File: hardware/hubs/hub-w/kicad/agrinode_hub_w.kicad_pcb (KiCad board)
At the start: 2 copper layers, 114 x 96 mm, 101 parts, among them J1 DC 12V 5.5/2.1, J2 DC IN 7-24V, J3 SOLAR 6-24V, J4 USB 5V / PROG, J5 BAT NTC 10k, J6 PROG, J7 I2C, J8 LED STRIP WS2813, J9 RS-485, Q1 AO3401A, Q2 AO3401A, Q3 MMBT3904, Q4 MMBT3904, Q5 BSS138, Q6 MMBT3904, SW1 RESET, SW2 BOOT / PAIR, U1 LM2596S-5.0, U2 TP4056, U3 MIC29302WU, U4 ESP32-WROOM-32E-N8, U5 CH340C, U6 DS3231MZ, U7 MAX3485ESA

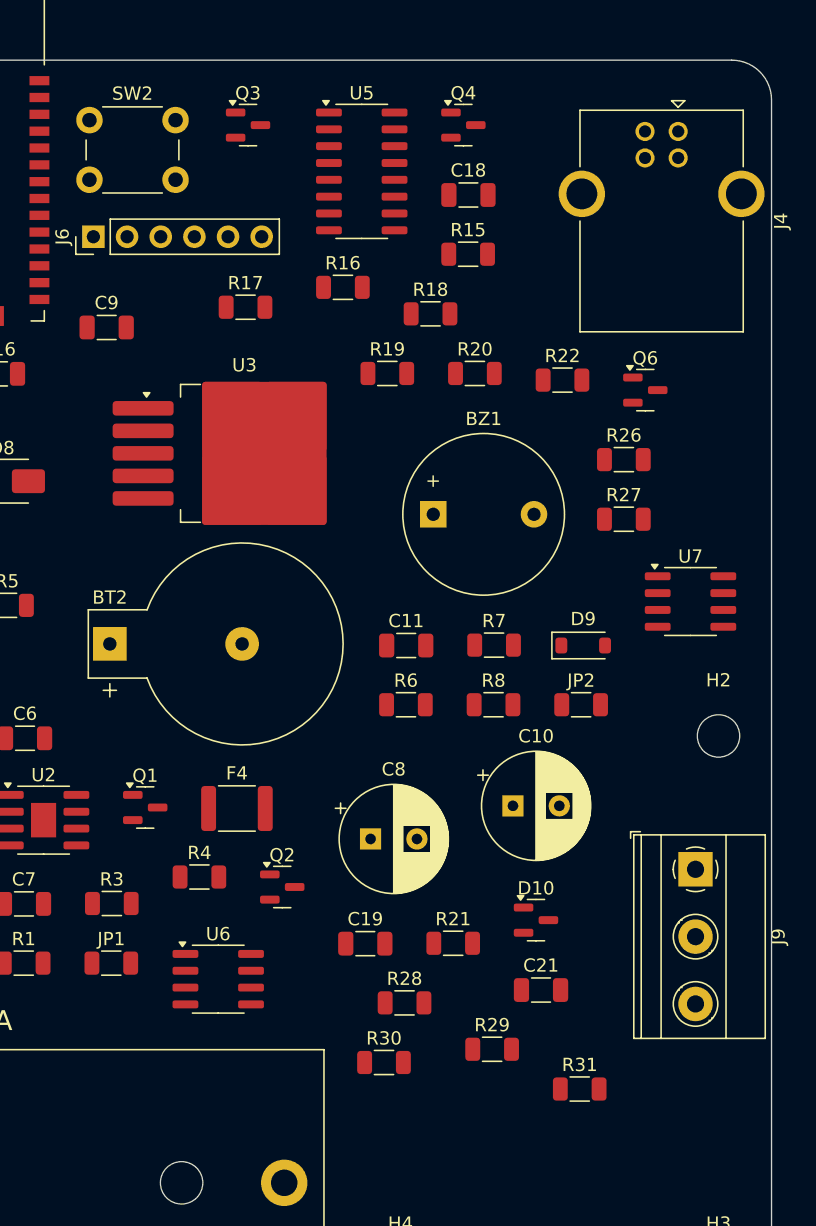
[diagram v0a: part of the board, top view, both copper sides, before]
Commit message: hubs: CH340C rotated so USB D+/D- face the USB-B jack; reroute in progress
Co-Authored-By: Claude Opus 5.5 <noreply@anthropic.com>
Claude-Session: https://claude.ai/code/session_014J7amXZ5Y6AZWEh5CjDNja
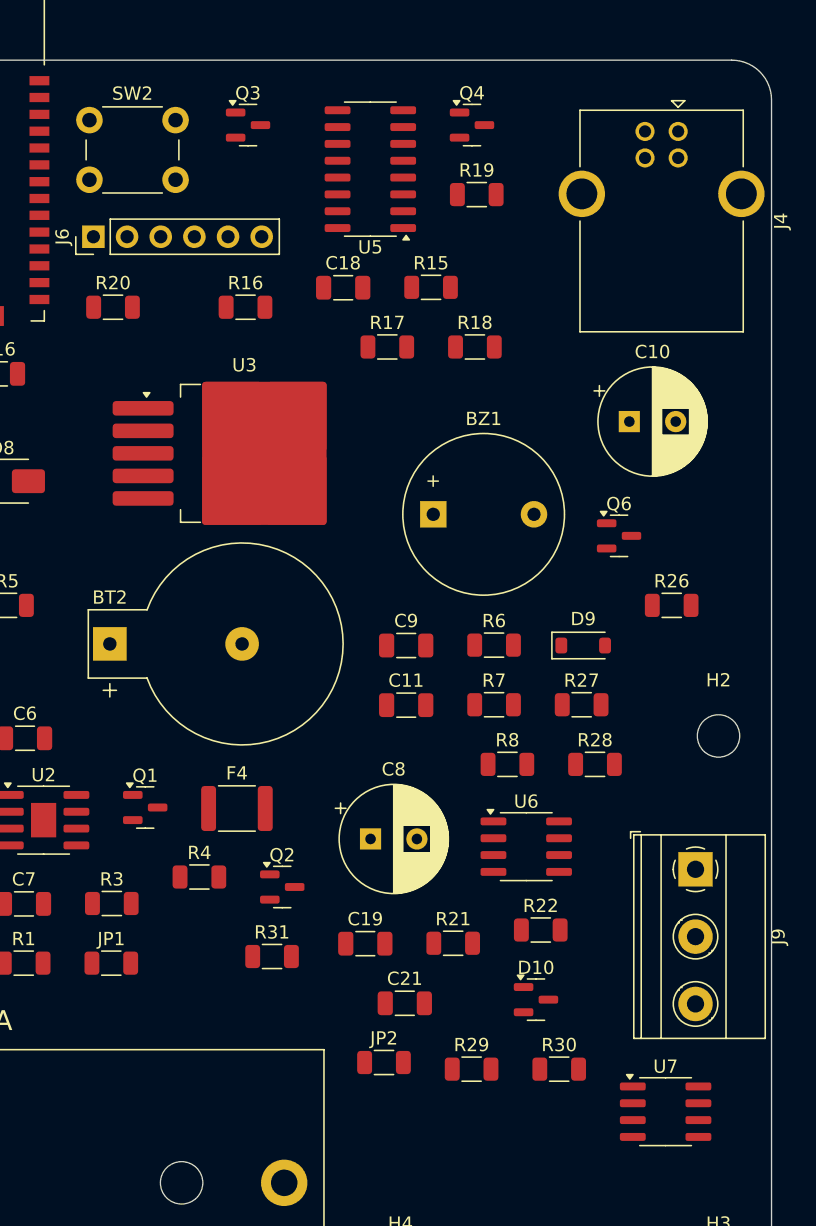
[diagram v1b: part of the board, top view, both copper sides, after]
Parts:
- moved R22 41.5 mm to (146.6, 115.6)
- moved U7 38.5 mm to (156.0, 129.4)
- moved C9 33.0 mm to (136.4, 94.2)
- moved JP2 30.8 mm to (134.8, 125.6)
- moved C10 30.3 mm to (153.3, 77.3)
- moved R20 27.8 mm to (114.3, 68.6)
- moved U6 25.3 mm to (145.5, 109.4)
- moved R31 25.3 mm to (126.3, 117.6)
- moved R28 23.0 mm to (150.7, 103.1)
- moved R19 15.1 mm to (141.8, 60.1)
- moved R27 14.4 mm to (149.7, 98.6)
- moved R30 13.2 mm to (148.0, 126.1)
- moved C18 11.8 mm to (131.7, 67.2)
- moved R26 11.6 mm to (156.5, 91.1)
- moved Q6 11.2 mm to (152.5, 85.9)
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
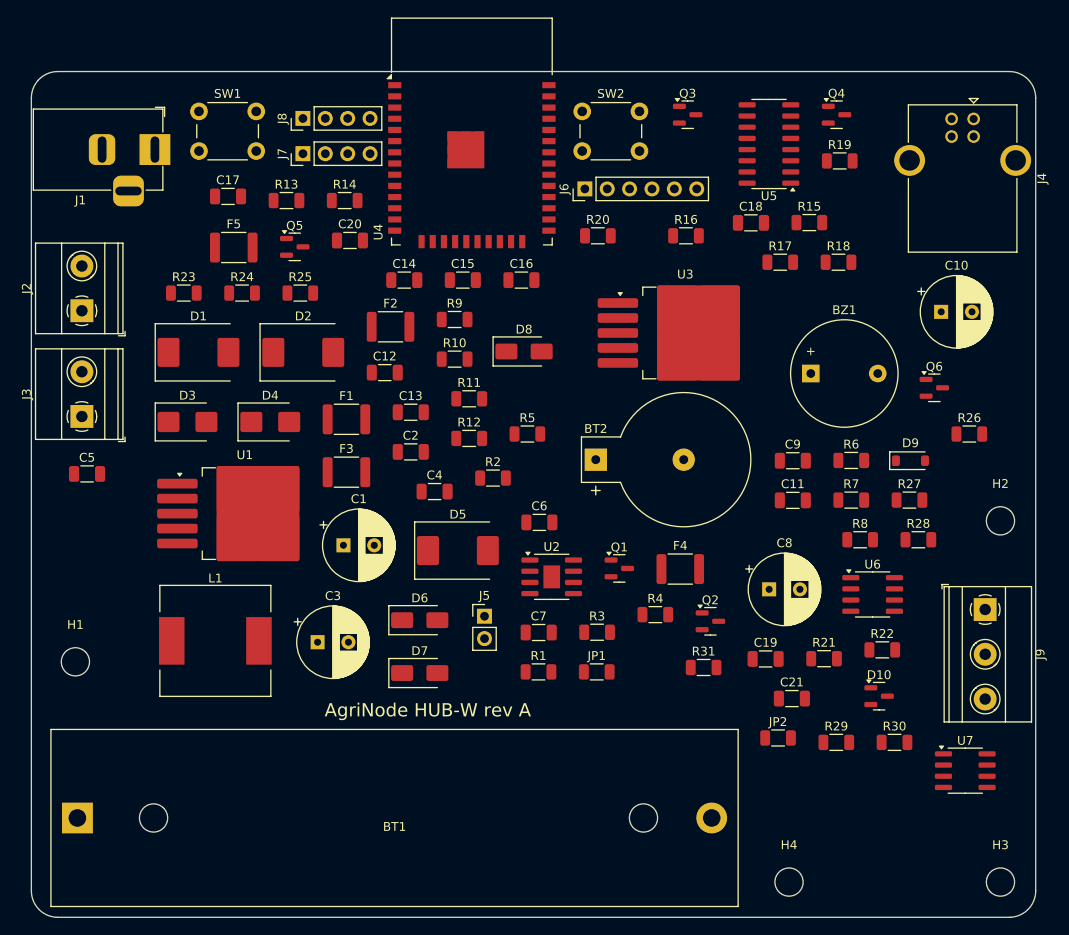
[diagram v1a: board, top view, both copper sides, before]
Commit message: hubs: routing progress snapshot (HUB-W 2 open, HUB-L 3 open)
Co-Authored-By: Claude Opus 5.5 <noreply@anthropic.com>
Claude-Session: https://claude.ai/code/session_014J7amXZ5Y6AZWEh5CjDNja
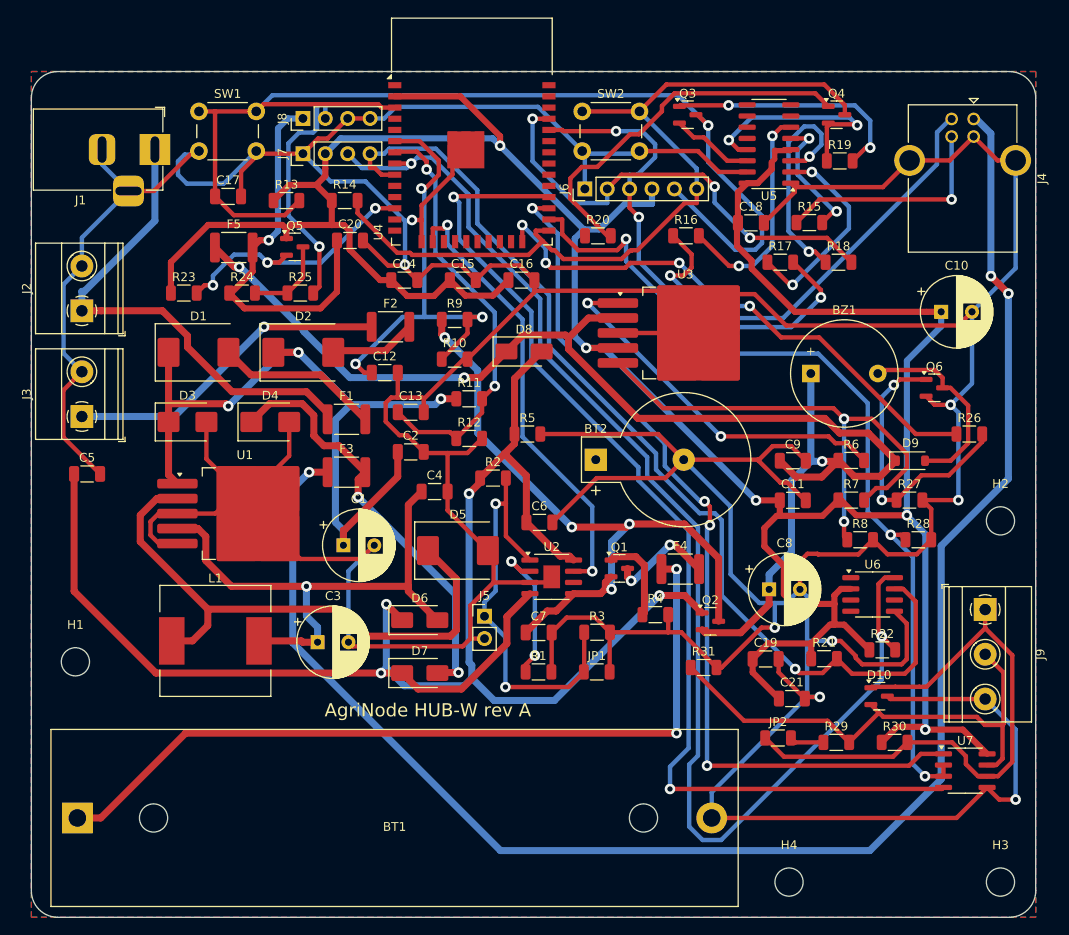
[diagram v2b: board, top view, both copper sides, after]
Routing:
- net GND: track 0.00 -> 802.5 mm, vias 0 -> 8
- net +3V3: track 0.00 -> 343.1 mm, vias 0 -> 5
- net /Power - 12V, solar and USB inputs, 18650 charger, rails/VUSB_RAW: track 0.00 -> 188.9 mm, vias 0 -> 3
- net /Power - 12V, solar and USB inputs, 18650 charger, rails/V5: track 0.00 -> 187.0 mm, vias 0 -> 4
- net VSYS: track 0.00 -> 155.3 mm, vias 0 -> 3
- net /ESP32, programming, buttons, RTC, LED strip, buzzer/I2C_SCL: track 0.00 -> 146.8 mm, vias 0 -> 2
- net /ESP32, programming, buttons, RTC, LED strip, buzzer/ESP_EN: track 0.00 -> 127.9 mm, vias 0 -> 1
- net RS485_TX: track 0.00 -> 121.1 mm, vias 0 -> 2
- net /ESP32, programming, buttons, RTC, LED strip, buzzer/I2C_SDA: track 0.00 -> 115.1 mm, vias 0 -> 1
- net RS485_RX: track 0.00 -> 101.3 mm, vias 0 -> 4
- net RS485_DE: track 0.00 -> 98.8 mm, vias 0 -> 3
- net /ESP32, programming, buttons, RTC, LED strip, buzzer/BOOT_BTN: track 0.00 -> 95.3 mm
- net /Power - 12V, solar and USB inputs, 18650 charger, rails/BATT_CELL: track 0.00 -> 92.3 mm, vias 0 -> 2
- net /Power - 12V, solar and USB inputs, 18650 charger, rails/VIN_BUCK: track 0.00 -> 86.5 mm, vias 0 -> 3
- net /Power - 12V, solar and USB inputs, 18650 charger, rails/VBAT: track 0.00 -> 77.0 mm, vias 0 -> 4
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- added copper zone on B.Cu, net GND
- added copper zone on F.Cu, net GND

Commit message: hubs: place DS3231 beside the CR2032 holder
Co-Authored-By: Claude Opus 5.5 <noreply@anthropic.com>
Claude-Session: https://claude.ai/code/session_014J7amXZ5Y6AZWEh5CjDNja
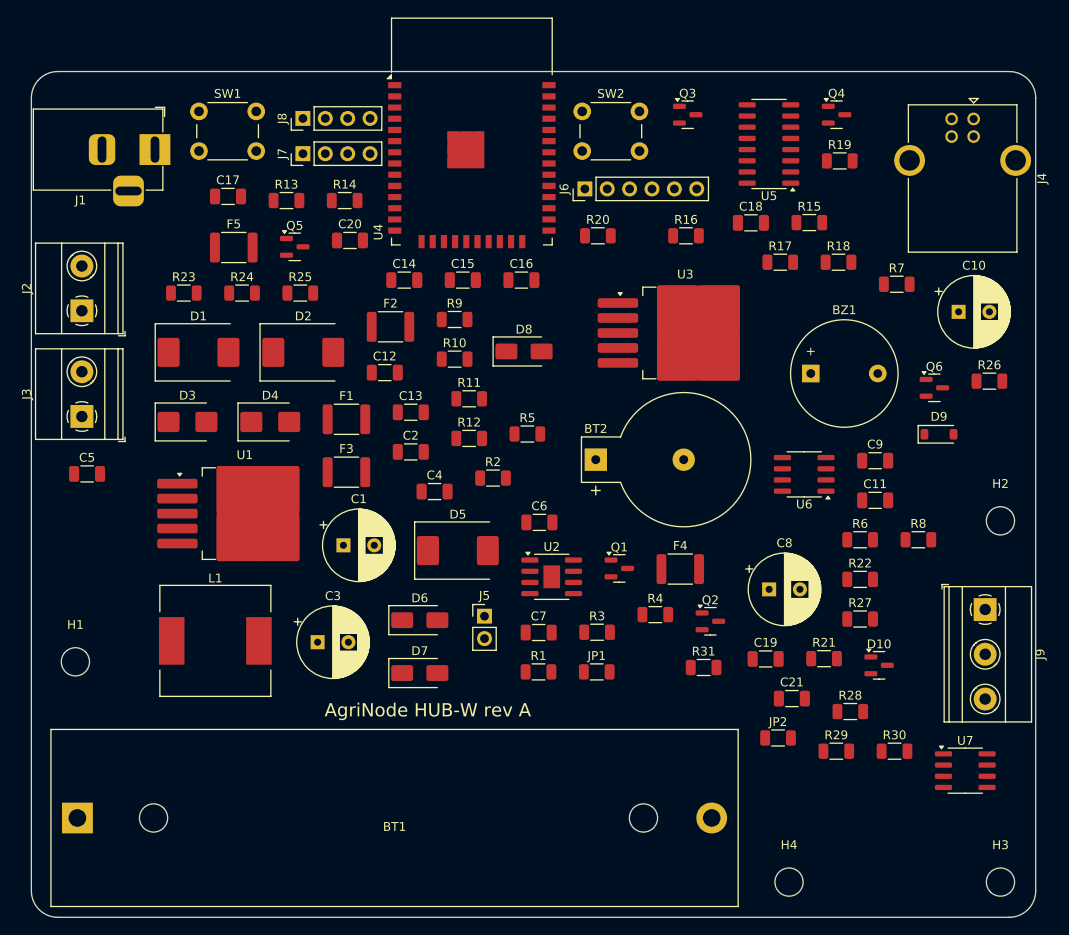
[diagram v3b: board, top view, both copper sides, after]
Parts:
- moved R7 25.0 mm to (148.2, 74.1)
- moved R28 21.0 mm to (143.0, 122.6)
- moved U6 15.7 mm to (137.7, 95.7), turned to 180 degrees
- moved R27 14.6 mm to (144.1, 112.1)
- moved C11 9.34 mm to (145.8, 98.7)
- moved C9 9.34 mm to (145.8, 94.2)
- moved R6 9.06 mm to (144.1, 103.1)
- moved R22 8.39 mm to (144.1, 107.6)
- moved R8 6.61 mm to (150.7, 103.1)
- moved R26 6.42 mm to (158.7, 85.1)
- moved D9 4.41 mm to (153.0, 91.2)
- moved D10 3.50 mm to (146.2, 117.4)
- moved C10 1.98 mm to (155.2, 77.3)
- moved R29 1.00 mm to (141.4, 127.1)
- moved R30 1.00 mm to (148.0, 127.1)
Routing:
- net GND: track 802.5 -> 0.00 mm, vias 8 -> 0
- net +3V3: track 343.1 -> 0.00 mm, vias 5 -> 0
- net /Power - 12V, solar and USB inputs, 18650 charger, rails/VUSB_RAW: track 188.9 -> 0.00 mm, vias 3 -> 0
- net /Power - 12V, solar and USB inputs, 18650 charger, rails/V5: track 187.0 -> 0.00 mm, vias 4 -> 0
- net VSYS: track 155.3 -> 0.00 mm, vias 3 -> 0
- net /ESP32, programming, buttons, RTC, LED strip, buzzer/I2C_SCL: track 146.8 -> 0.00 mm, vias 2 -> 0
- net /ESP32, programming, buttons, RTC, LED strip, buzzer/ESP_EN: track 127.9 -> 0.00 mm, vias 1 -> 0
- net RS485_TX: track 121.1 -> 0.00 mm, vias 2 -> 0
- net /ESP32, programming, buttons, RTC, LED strip, buzzer/I2C_SDA: track 115.1 -> 0.00 mm, vias 1 -> 0
- net RS485_RX: track 101.3 -> 0.00 mm, vias 4 -> 0
- net RS485_DE: track 98.8 -> 0.00 mm, vias 3 -> 0
- net /ESP32, programming, buttons, RTC, LED strip, buzzer/BOOT_BTN: track 95.3 -> 0.00 mm
- net /Power - 12V, solar and USB inputs, 18650 charger, rails/BATT_CELL: track 92.3 -> 0.00 mm, vias 2 -> 0
- net /Power - 12V, solar and USB inputs, 18650 charger, rails/VIN_BUCK: track 86.5 -> 0.00 mm, vias 3 -> 0
- net /Power - 12V, solar and USB inputs, 18650 charger, rails/VBAT: track 77.0 -> 0.00 mm, vias 4 -> 0
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- removed copper zone on B.Cu, net GND
- removed copper zone on F.Cu, net GND

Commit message: HUB-W: fully routed (0 unconnected, 0 clearance errors), renders and Gerbers
Co-Authored-By: Claude Opus 5.5 <noreply@anthropic.com>
Claude-Session: https://claude.ai/code/session_014J7amXZ5Y6AZWEh5CjDNja
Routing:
- net GND: track 0.00 -> 753.0 mm, vias 0 -> 9
- net +3V3: track 0.00 -> 330.4 mm, vias 0 -> 13
- net /Power - 12V, solar and USB inputs, 18650 charger, rails/V5: track 0.00 -> 166.7 mm
- net VSYS: track 0.00 -> 156.8 mm, vias 0 -> 2
- net RS485_DE: track 0.00 -> 123.7 mm, vias 0 -> 3
- net /ESP32, programming, buttons, RTC, LED strip, buzzer/ESP_EN: track 0.00 -> 121.2 mm, vias 0 -> 3
- net /Power - 12V, solar and USB inputs, 18650 charger, rails/VUSB_RAW: track 0.00 -> 120.7 mm, vias 0 -> 3
- net RS485_RX: track 0.00 -> 116.2 mm, vias 0 -> 4
- net /ESP32, programming, buttons, RTC, LED strip, buzzer/I2C_SDA: track 0.00 -> 109.1 mm, vias 0 -> 5
- net VIN_ADC: track 0.00 -> 105.1 mm, vias 0 -> 2
- net RS485_TX: track 0.00 -> 104.9 mm, vias 0 -> 2
- net /ESP32, programming, buttons, RTC, LED strip, buzzer/I2C_SCL: track 0.00 -> 93.0 mm, vias 0 -> 3
- net /ESP32, programming, buttons, RTC, LED strip, buzzer/BOOT_BTN: track 0.00 -> 91.1 mm, vias 0 -> 2
- net /Power - 12V, solar and USB inputs, 18650 charger, rails/LDO3_ADJ: track 0.00 -> 87.5 mm, vias 0 -> 3
- net /Power - 12V, solar and USB inputs, 18650 charger, rails/VIN_BUCK: track 0.00 -> 85.2 mm, vias 0 -> 1
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- added copper zone on B.Cu, net GND
- added copper zone on F.Cu, net GND

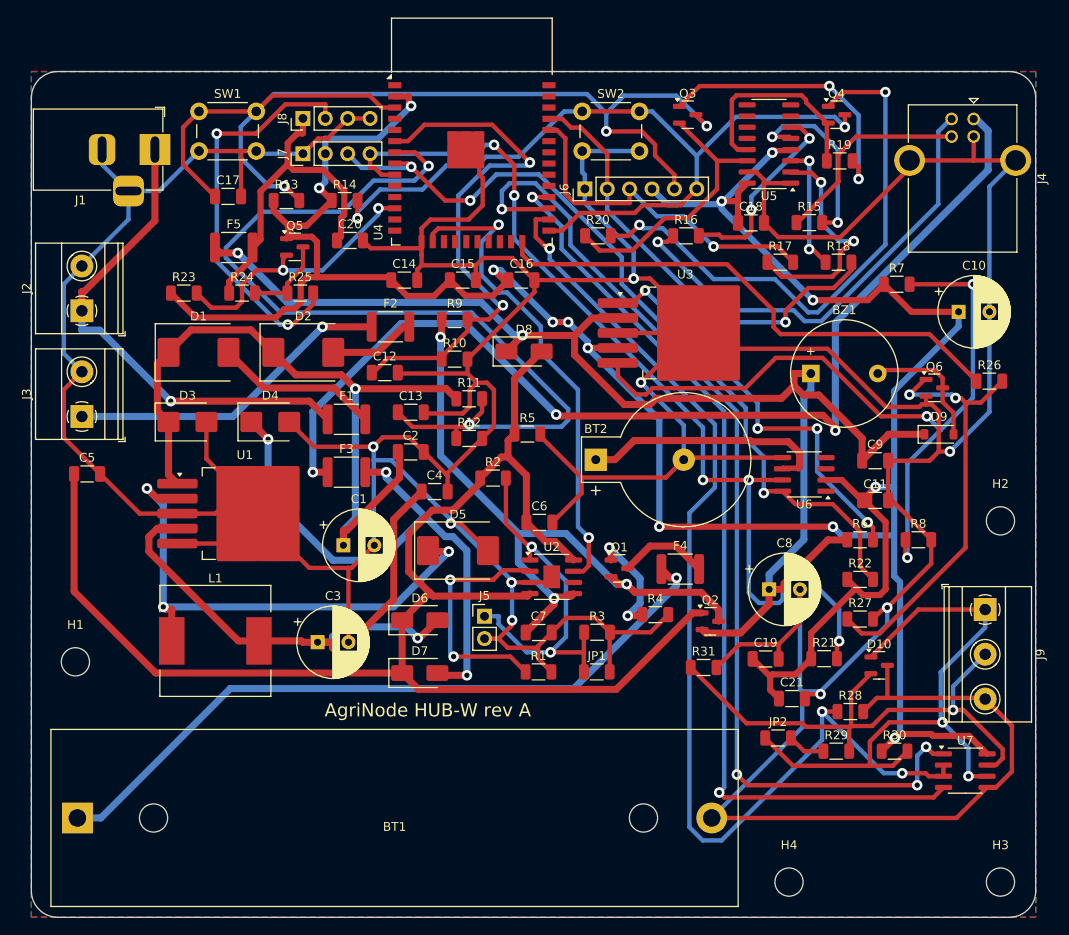
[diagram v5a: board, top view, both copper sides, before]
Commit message: hubs: open a 6 mm routing channel beside the ESP32 right column (BOOT button and PROG header moved); pin the LDO bulk cap
Co-Authored-By: Claude Opus 5.5 <noreply@anthropic.com>
Claude-Session: https://claude.ai/code/session_014J7amXZ5Y6AZWEh5CjDNja
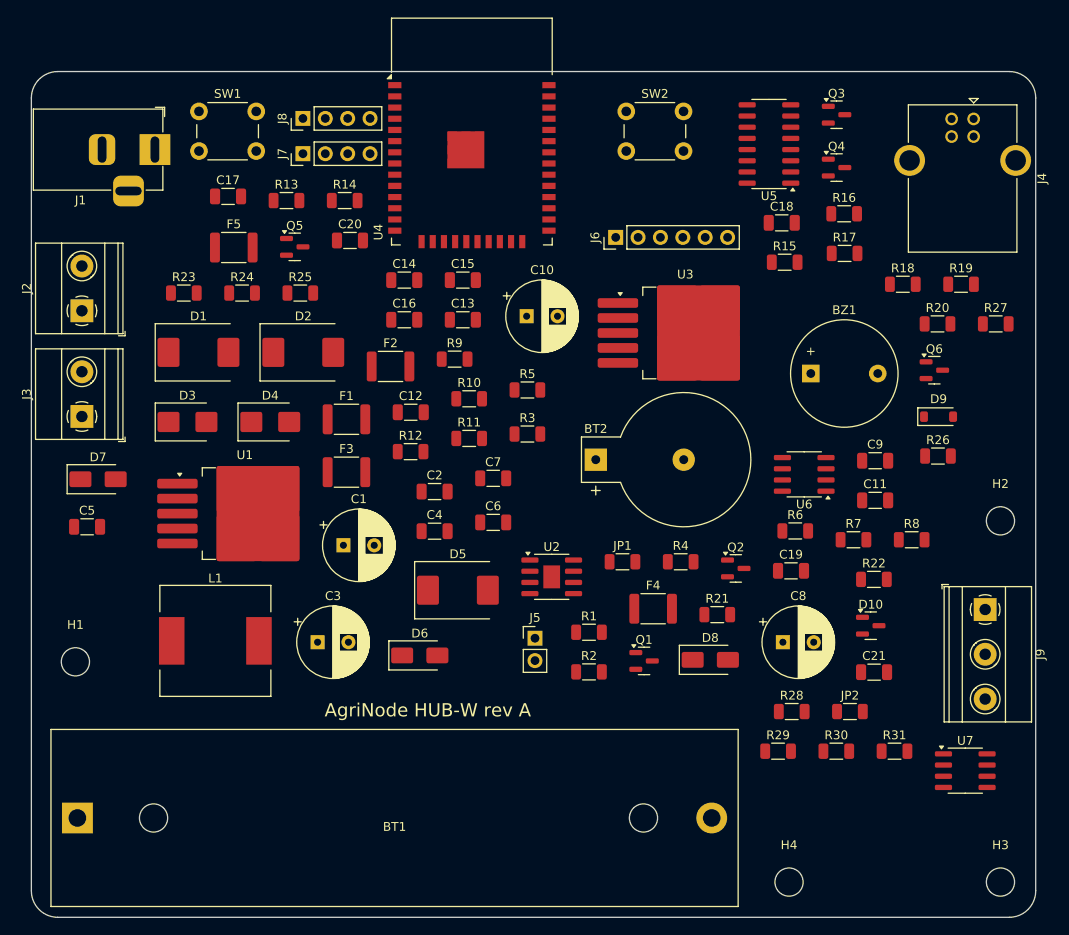
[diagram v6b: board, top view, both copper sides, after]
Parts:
- moved C10 49.0 mm to (106.2, 77.8)
- moved D7 42.6 mm to (57.6, 96.3)
- moved D8 40.9 mm to (127.1, 116.8)
- moved R20 39.8 mm to (152.9, 78.6)
- moved R27 36.9 mm to (159.5, 78.6)
- moved R7 29.4 mm to (143.3, 103.1)
- moved R2 24.5 mm to (113.3, 118.1)
- moved R3 23.8 mm to (106.3, 91.1)
- moved R31 23.7 mm to (148.0, 127.1)
- moved R19 19.6 mm to (155.5, 74.1)
- moved C7 18.2 mm to (102.4, 96.2)
- moved R16 18.1 mm to (142.3, 66.1)
- moved Q3 16.9 mm to (141.4, 54.9)
- moved C16 14.0 mm to (92.3, 78.2)
- moved R21 13.1 mm to (127.9, 111.6)
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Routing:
- net GND: track 753.0 -> 0.00 mm, vias 9 -> 0
- net +3V3: track 330.4 -> 0.00 mm, vias 13 -> 0
- net /Power - 12V, solar and USB inputs, 18650 charger, rails/V5: track 166.7 -> 0.00 mm
- net VSYS: track 156.8 -> 0.00 mm, vias 2 -> 0
- net RS485_DE: track 123.7 -> 0.00 mm, vias 3 -> 0
- net /ESP32, programming, buttons, RTC, LED strip, buzzer/ESP_EN: track 121.2 -> 0.00 mm, vias 3 -> 0
- net /Power - 12V, solar and USB inputs, 18650 charger, rails/VUSB_RAW: track 120.7 -> 0.00 mm, vias 3 -> 0
- net RS485_RX: track 116.2 -> 0.00 mm, vias 4 -> 0
- net /ESP32, programming, buttons, RTC, LED strip, buzzer/I2C_SDA: track 109.1 -> 0.00 mm, vias 5 -> 0
- net VIN_ADC: track 105.1 -> 0.00 mm, vias 2 -> 0
- net RS485_TX: track 104.9 -> 0.00 mm, vias 2 -> 0
- net /ESP32, programming, buttons, RTC, LED strip, buzzer/I2C_SCL: track 93.0 -> 0.00 mm, vias 3 -> 0
- net /ESP32, programming, buttons, RTC, LED strip, buzzer/BOOT_BTN: track 91.1 -> 0.00 mm, vias 2 -> 0
- net /Power - 12V, solar and USB inputs, 18650 charger, rails/LDO3_ADJ: track 87.5 -> 0.00 mm, vias 3 -> 0
- net /Power - 12V, solar and USB inputs, 18650 charger, rails/VIN_BUCK: track 85.2 -> 0.00 mm, vias 1 -> 0
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- removed copper zone on B.Cu, net GND
- removed copper zone on F.Cu, net GND
